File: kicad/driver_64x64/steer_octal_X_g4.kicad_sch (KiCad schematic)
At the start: 66 parts

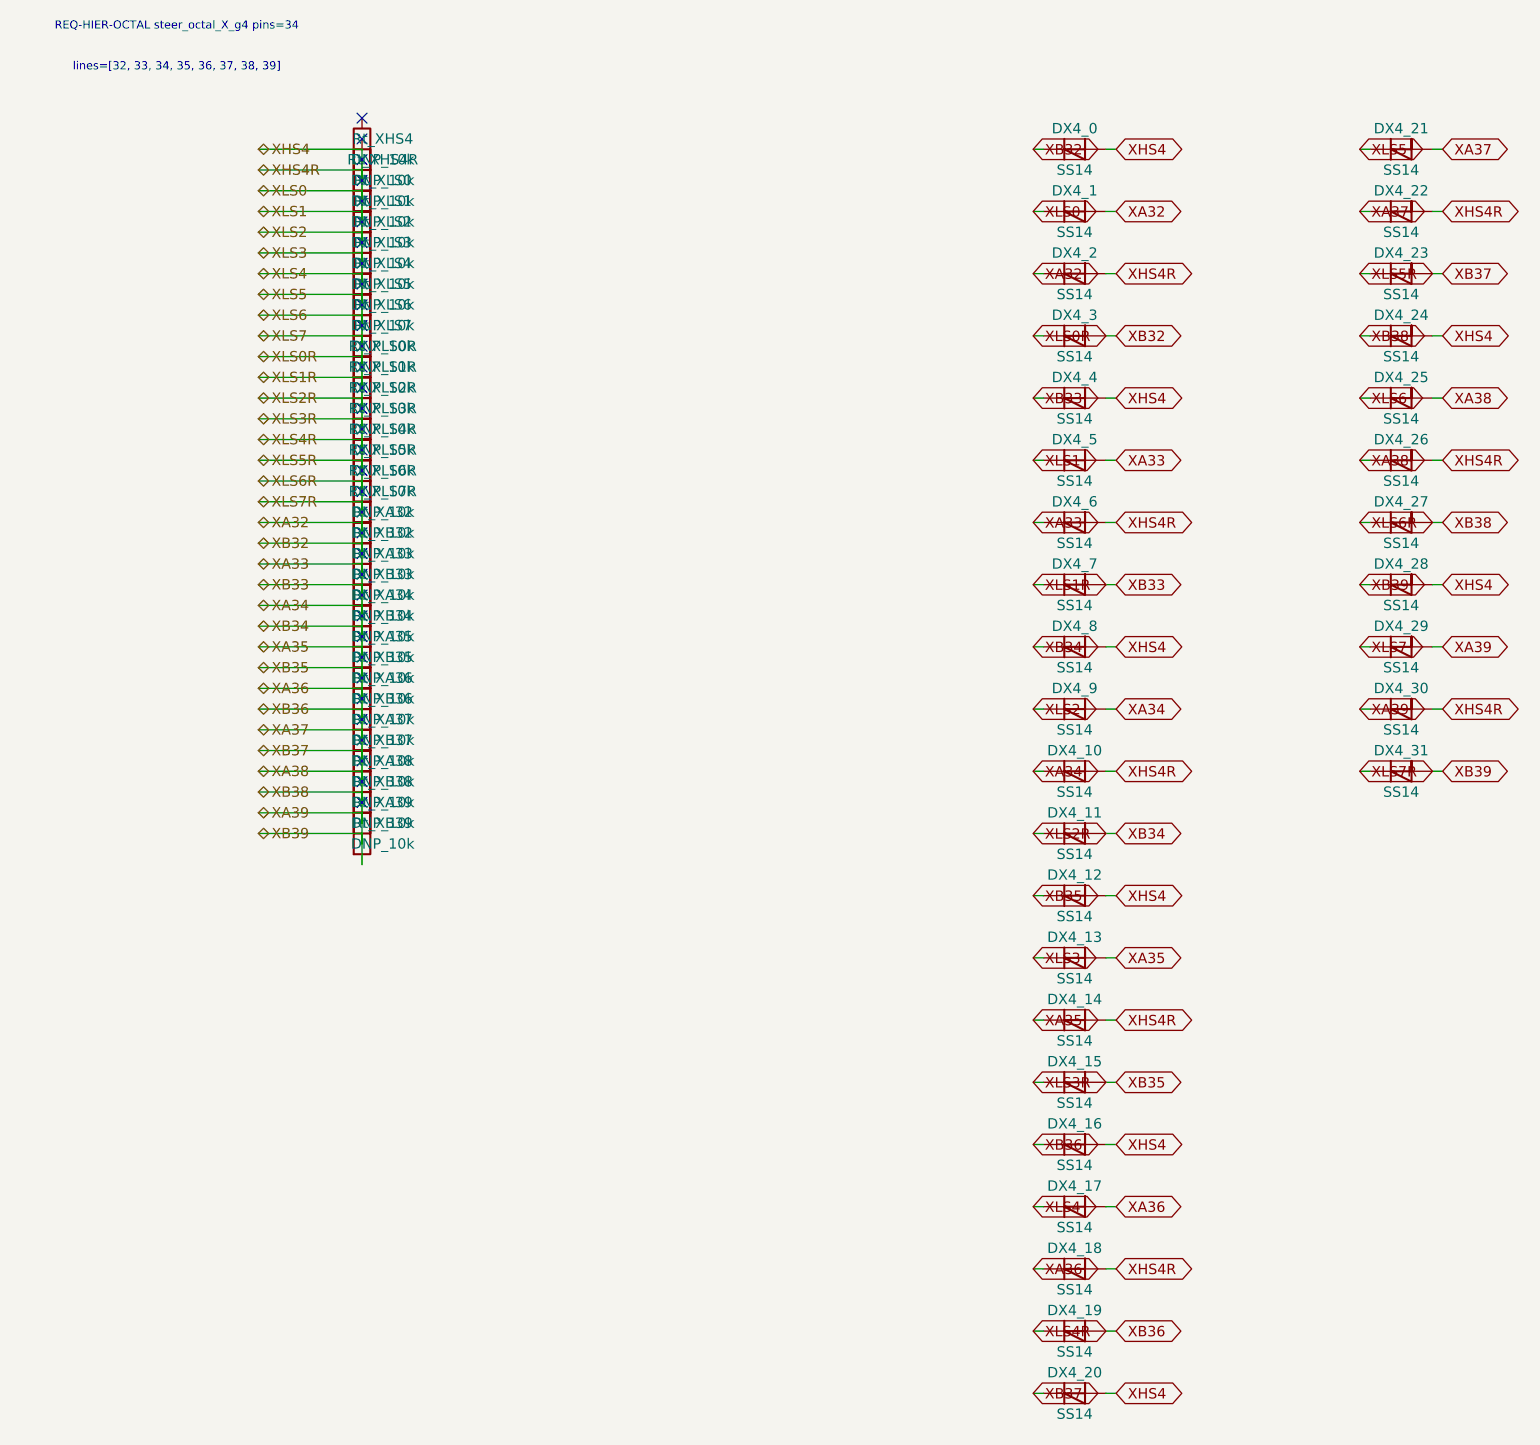
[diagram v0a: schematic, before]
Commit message: logical seperation into host and multiple decode/drive/steering boards
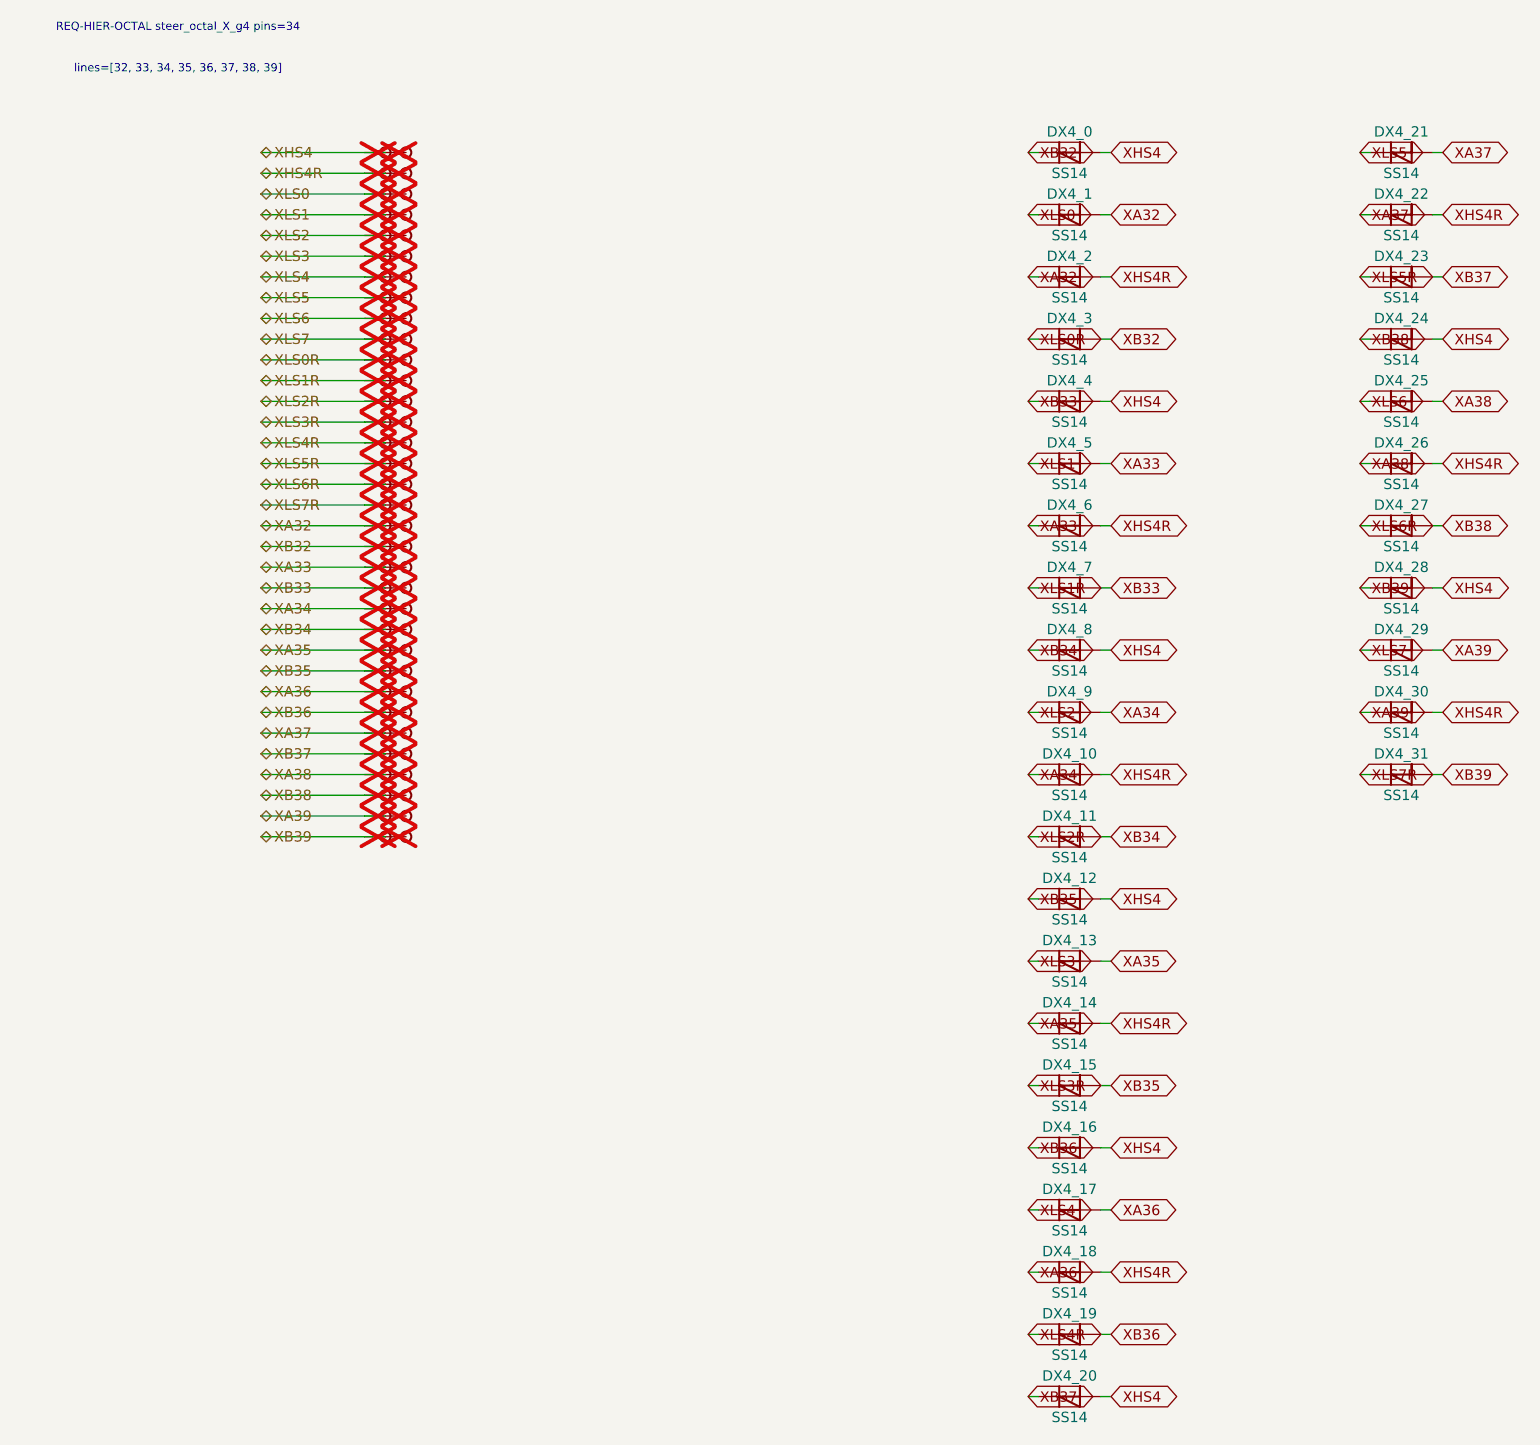
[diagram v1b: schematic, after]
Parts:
- removed Rt_XA32, Rt_XA33, Rt_XA34, Rt_XA35, Rt_XA36, Rt_XA37, Rt_XA38, Rt_XA39, Rt_XB32, Rt_XB33, Rt_XB34, Rt_XB35, Rt_XB36, Rt_XB37, Rt_XB38, Rt_XB39, Rt_XHS4, Rt_XHS4R, Rt_XLS0, Rt_XLS0R, Rt_XLS1, Rt_XLS1R, Rt_XLS2, Rt_XLS2R, Rt_XLS3, Rt_XLS3R, Rt_XLS4, Rt_XLS4R, Rt_XLS5, Rt_XLS5R, Rt_XLS6, Rt_XLS6R, Rt_XLS7, Rt_XLS7R: DNP_10k, symbol Device:R
- added TP_XA32, TP_XA32b, TP_XA33, TP_XA33b, TP_XA34, TP_XA34b, TP_XA35, TP_XA35b, TP_XA36, TP_XA36b, TP_XA37, TP_XA37b, TP_XA38, TP_XA38b, TP_XA39, TP_XA39b, TP_XB32, TP_XB32b, TP_XB33, TP_XB33b, TP_XB34, TP_XB34b, TP_XB35, TP_XB35b, TP_XB36, TP_XB36b, TP_XB37, TP_XB37b, TP_XB38, TP_XB38b, TP_XB39, TP_XB39b, TP_XHS4, TP_XHS4R, TP_XHS4Rb, TP_XHS4b, TP_XLS0, TP_XLS0R, TP_XLS0Rb, TP_XLS0b, TP_XLS1, TP_XLS1R, TP_XLS1Rb, TP_XLS1b, TP_XLS2, TP_XLS2R, TP_XLS2Rb, TP_XLS2b, TP_XLS3, TP_XLS3R, TP_XLS3Rb, TP_XLS3b, TP_XLS4, TP_XLS4R, TP_XLS4Rb, TP_XLS4b, TP_XLS5, TP_XLS5R, TP_XLS5Rb, TP_XLS5b, TP_XLS6, TP_XLS6R, TP_XLS6Rb, TP_XLS6b, TP_XLS7, TP_XLS7R, TP_XLS7Rb, TP_XLS7b: Stub, symbol CMR:Stub
- DX4_0, DX4_1, DX4_10, DX4_11, DX4_12, DX4_13, DX4_14, DX4_15, DX4_16, DX4_17, DX4_18, DX4_19, DX4_2, DX4_20, DX4_21, DX4_22, DX4_23, DX4_24, DX4_25, DX4_26, DX4_27, DX4_28, DX4_29, DX4_3, DX4_30, DX4_31, DX4_4, DX4_5, DX4_6, DX4_7, DX4_8, DX4_9: symbol Device:D_Schottky -> CMR:D_Schottky
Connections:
- net XA32: now also TP_XA32.1, TP_XA32b.1; no longer DX4_0.1 (K), DX4_0.2 (A), DX4_1.1 (K), DX4_10.1 (K), DX4_10.2 (A), DX4_11.1 (K), DX4_11.2 (A), DX4_12.1 (K), DX4_12.2 (A), DX4_13.1 (K), DX4_13.2 (A), DX4_14.1 (K), DX4_14.2 (A), DX4_15.1 (K), DX4_15.2 (A), DX4_16.1 (K), DX4_16.2 (A), DX4_17.1 (K), DX4_17.2 (A), DX4_18.1 (K), DX4_18.2 (A), DX4_19.1 (K), DX4_19.2 (A), DX4_2.2 (A), DX4_20.1 (K), DX4_20.2 (A), DX4_21.1 (K), DX4_21.2 (A), DX4_22.1 (K), DX4_22.2 (A), DX4_23.1 (K), DX4_23.2 (A), DX4_24.1 (K), DX4_24.2 (A), DX4_25.1 (K), DX4_25.2 (A), DX4_26.1 (K), DX4_26.2 (A), DX4_27.1 (K), DX4_27.2 (A), DX4_28.1 (K), DX4_28.2 (A), DX4_29.1 (K), DX4_29.2 (A), DX4_3.1 (K), DX4_3.2 (A), DX4_30.1 (K), DX4_30.2 (A), DX4_31.1 (K), DX4_31.2 (A), DX4_4.1 (K), DX4_4.2 (A), DX4_5.1 (K), DX4_5.2 (A), DX4_6.1 (K), DX4_6.2 (A), DX4_7.1 (K), DX4_7.2 (A), DX4_8.1 (K), DX4_8.2 (A), DX4_9.1 (K), DX4_9.2 (A)
- new net XA33: DX4_5.2 (A), DX4_6.1 (K), TP_XA33.1, TP_XA33b.1
- new net XA34: DX4_10.1 (K), DX4_9.2 (A), TP_XA34.1, TP_XA34b.1
- new net XA35: DX4_13.2 (A), DX4_14.1 (K), TP_XA35.1, TP_XA35b.1
- new net XA36: DX4_17.2 (A), DX4_18.1 (K), TP_XA36.1, TP_XA36b.1
- new net XA37: DX4_21.2 (A), DX4_22.1 (K), TP_XA37.1, TP_XA37b.1
- new net XA38: DX4_25.2 (A), DX4_26.1 (K), TP_XA38.1, TP_XA38b.1
- new net XA39: DX4_29.2 (A), DX4_30.1 (K), TP_XA39.1, TP_XA39b.1
- new net XB32: DX4_0.1 (K), DX4_3.2 (A), TP_XB32.1, TP_XB32b.1
- new net XB33: DX4_4.1 (K), DX4_7.2 (A), TP_XB33.1, TP_XB33b.1
- new net XB34: DX4_11.2 (A), DX4_8.1 (K), TP_XB34.1, TP_XB34b.1
- new net XB35: DX4_12.1 (K), DX4_15.2 (A), TP_XB35.1, TP_XB35b.1
- new net XB36: DX4_16.1 (K), DX4_19.2 (A), TP_XB36.1, TP_XB36b.1
- new net XB37: DX4_20.1 (K), DX4_23.2 (A), TP_XB37.1, TP_XB37b.1
- new net XB38: DX4_24.1 (K), DX4_27.2 (A), TP_XB38.1, TP_XB38b.1
- new net XB39: DX4_28.1 (K), DX4_31.2 (A), TP_XB39.1, TP_XB39b.1
- new net XHS4: DX4_0.2 (A), DX4_12.2 (A), DX4_16.2 (A), DX4_20.2 (A), DX4_24.2 (A), DX4_28.2 (A), DX4_4.2 (A), DX4_8.2 (A), TP_XHS4.1, TP_XHS4b.1
- new net XHS4R: DX4_10.2 (A), DX4_14.2 (A), DX4_18.2 (A), DX4_2.2 (A), DX4_22.2 (A), DX4_26.2 (A), DX4_30.2 (A), DX4_6.2 (A), TP_XHS4R.1, TP_XHS4Rb.1
- new net XLS0: DX4_1.1 (K), TP_XLS0.1, TP_XLS0b.1
- new net XLS0R: DX4_3.1 (K), TP_XLS0R.1, TP_XLS0Rb.1
- new net XLS1: DX4_5.1 (K), TP_XLS1.1, TP_XLS1b.1
- new net XLS1R: DX4_7.1 (K), TP_XLS1R.1, TP_XLS1Rb.1
- new net XLS2: DX4_9.1 (K), TP_XLS2.1, TP_XLS2b.1
- new net XLS2R: DX4_11.1 (K), TP_XLS2R.1, TP_XLS2Rb.1
- new net XLS3: DX4_13.1 (K), TP_XLS3.1, TP_XLS3b.1
- new net XLS3R: DX4_15.1 (K), TP_XLS3R.1, TP_XLS3Rb.1
- new net XLS4: DX4_17.1 (K), TP_XLS4.1, TP_XLS4b.1
- new net XLS4R: DX4_19.1 (K), TP_XLS4R.1, TP_XLS4Rb.1
- new net XLS5: DX4_21.1 (K), TP_XLS5.1, TP_XLS5b.1
- new net XLS5R: DX4_23.1 (K), TP_XLS5R.1, TP_XLS5Rb.1
- new net XLS6: DX4_25.1 (K), TP_XLS6.1, TP_XLS6b.1
- new net XLS6R: DX4_27.1 (K), TP_XLS6R.1, TP_XLS6Rb.1
- new net XLS7: DX4_29.1 (K), TP_XLS7.1, TP_XLS7b.1
- new net XLS7R: DX4_31.1 (K), TP_XLS7R.1, TP_XLS7Rb.1
- no-connect marks 34 -> 0
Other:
- moved on the sheet: DX4_0, DX4_1, DX4_10, DX4_11, DX4_12, DX4_13, DX4_14, DX4_15, DX4_16, DX4_17, DX4_18, DX4_19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
